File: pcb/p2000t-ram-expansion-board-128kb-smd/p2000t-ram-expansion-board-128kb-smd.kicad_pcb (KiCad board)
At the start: 2 copper layers, 110 x 45.5 mm, 24 parts, among them J1 EXPANSION BOARD, J2 POWER, J3 TERMINAL, U1 74HC138, U10 74HC02, U2 62128, U3 74HC00, U4 74HC283, U5 74HC138, U7 74HC173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

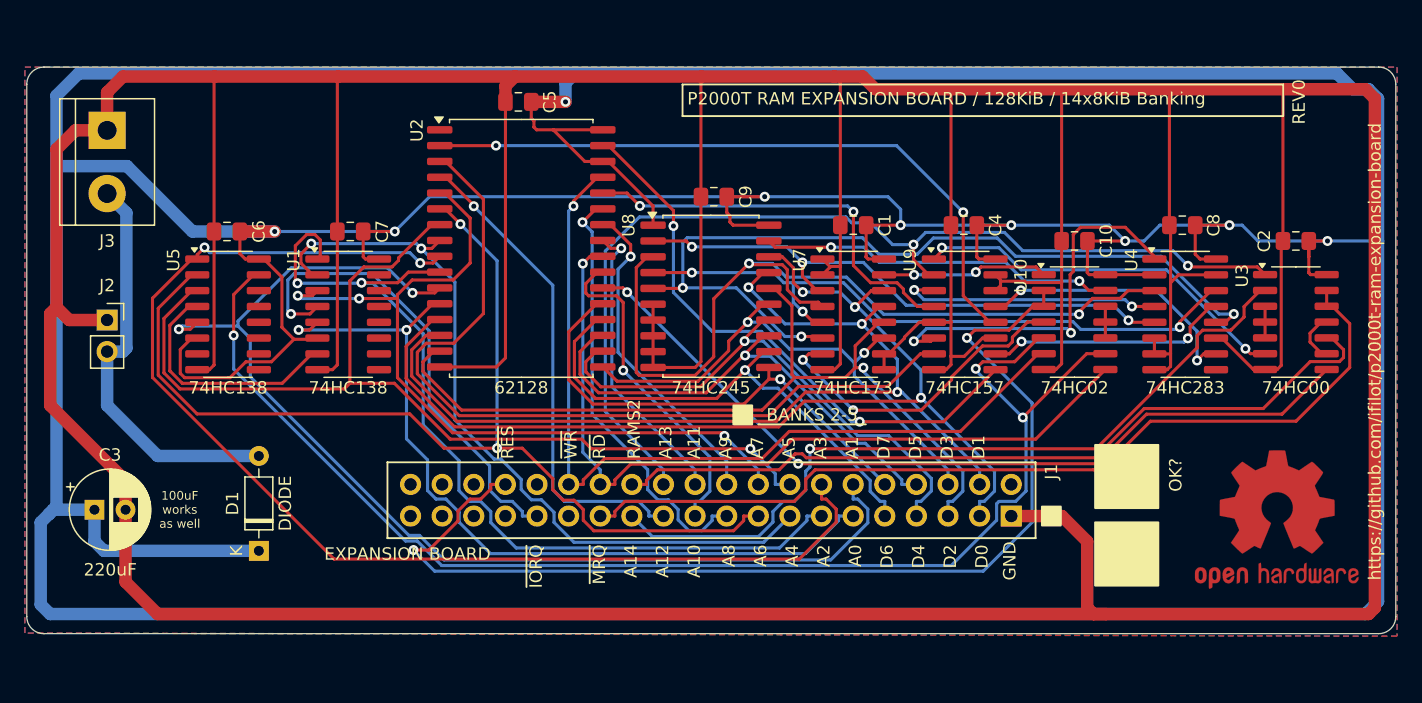
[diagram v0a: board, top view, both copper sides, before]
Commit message: Changing silk screen
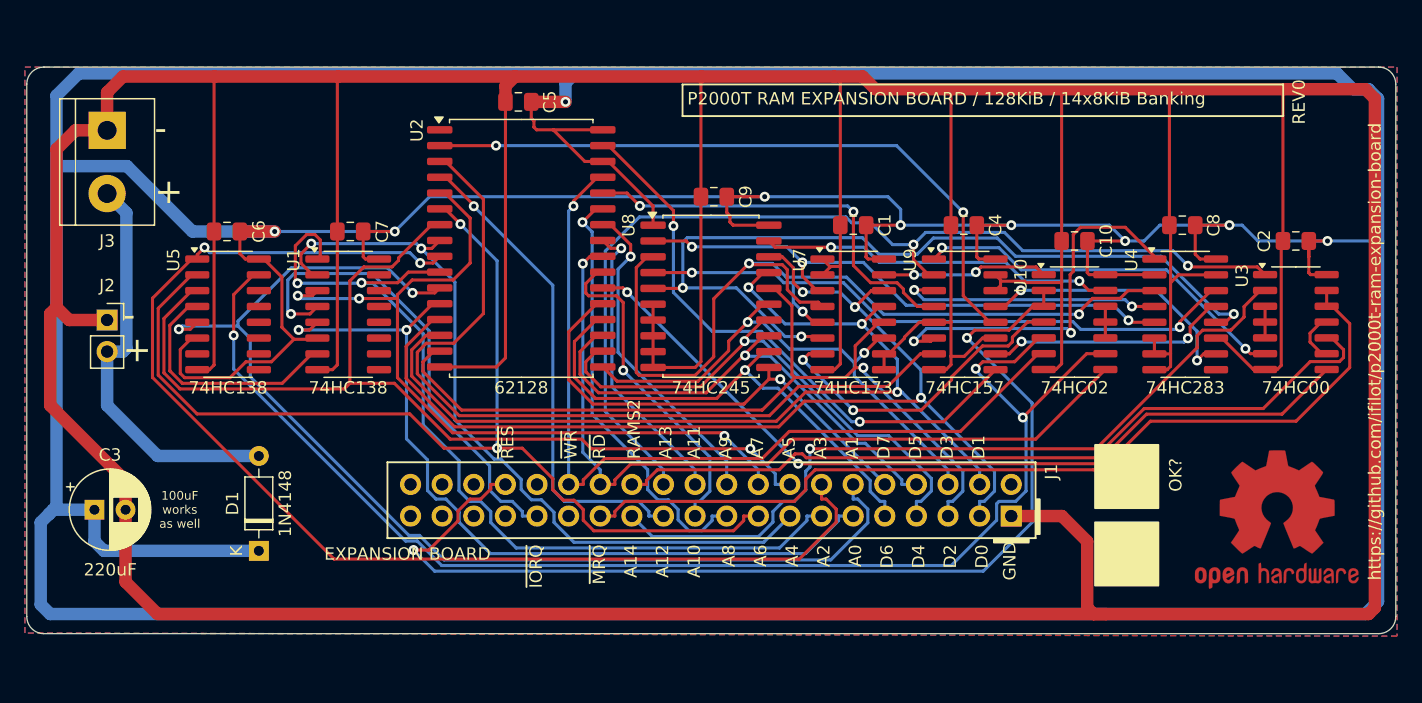
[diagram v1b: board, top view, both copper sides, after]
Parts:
- D1: value DIODE -> 1N4148
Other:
- board text added: "+"
- board text added: "-"
- board text removed: "BANKS 2-5"
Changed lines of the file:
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@@
 			)
 		)
-		(property "Value" "DIODE"
+		(property "Value" "1N4148"
 			(at 3.81 2.12 -90)
 			(layer "F.SilkS")
@@
 		)
 	)
-	(gr_line
-		(start 78.74 73.152)
-		(end 87.376 73.152)
-		(stroke
-			(width 0.15)
-			(type solid)
-		)
-		(layer "F.SilkS")
-	)
 	(gr_rect
-		(start 105.791 74.803)
-		(end 110.871 79.883)
+		(start 97.663 82.3976)
+		(end 100.457 82.6516)
 		(stroke
 			(width 0.15)
@@
 	)
 	(gr_rect
-		(start 76.723 71.628)
-		(end 78.247 73.152)
+		(start 105.791 74.803)
+		(end 110.871 79.883)
 		(stroke
 			(width 0.15)
@@
 	)
 	(gr_rect
-		(start 101.516 79.756)
-		(end 103.04 81.28)
+		(start 101.092 79.1718)
+		(end 101.346 81.9658)
 		(stroke
 			(width 0.15)
@@
 		)
 	)
+	(gr_text "-"
+		(at 27.686 65.532 0)
+		(layer "F.SilkS")
+		(effects
+			(font
+				(size 2 2)
+				(thickness 0.2)
+			)
+			(justify left bottom)
+		)
+	)
 	(gr_text "A3"
 		(at 83.736 75.946 90)
@@
 		)
 	)
+	(gr_text "+"
+		(at 30.226 55.626 0)
+		(layer "F.SilkS")
+		(effects
+			(font
+				(size 2 2)
+				(thickness 0.2)
+			)
+			(justify left bottom)
+		)
+	)
 	(gr_text "A8"
 		(at 76.37 82.804 90)
@@
 		)
 	)
-	(gr_text "BANKS 2-5"
-		(at 83.058 72.39 0)
+	(gr_text "+"
+		(at 27.686 68.326 0)
 		(layer "F.SilkS")
 		(effects
 			(font
-				(size 1 1)
-				(thickness 0.15)
+				(size 2 2)
+				(thickness 0.2)
 			)
+			(justify left bottom)
 		)
 	)
@@
 		)
 	)
+	(gr_text "-"
+		(at 30.226 50.546 0)
+		(layer "F.SilkS")
+		(effects
+			(font
+				(size 2 2)
+				(thickness 0.2)
+			)
+			(justify left bottom)
+		)
+	)

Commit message: Revising board layout
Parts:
- added G***: LOGO, components:ram-stick-logo, F.Cu at (41.0, 50.9)
- moved LOGO1 1.53 mm to (118.9, 80.6)
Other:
- board text added: "DATE"
- board text added: "REV1"
- board text removed: "REV0"
